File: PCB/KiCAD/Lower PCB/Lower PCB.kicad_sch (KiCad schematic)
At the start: 118 parts, among them IC1 ADG608BRZ, IC2 ADG608BRZ, IC3 ADG608BRZ, J1 Conn_01x04_MountingPin, J2 Conn_01x04_MountingPin, J3 Conn_01x04_MountingPin, J4 Conn_01x02_MountingPin, Q1 SFH320, Q10 SFH320, Q11 SFH320, Q12 SFH320, Q13 SFH320, Q14 SFH320, Q15 SFH320, Q16 SFH320, Q17 SFH320, Q18 SFH320, Q19 SFH320, Q2 SFH320, Q20 SFH320, Q21 SFH320, Q22 SFH320, Q23 SFH320, Q24 SFH320, Q3 SFH320, Q4 SFH320, Q5 SFH320, Q6 SFH320, Q7 SFH320, Q8 SFH320, Q9 SFH320

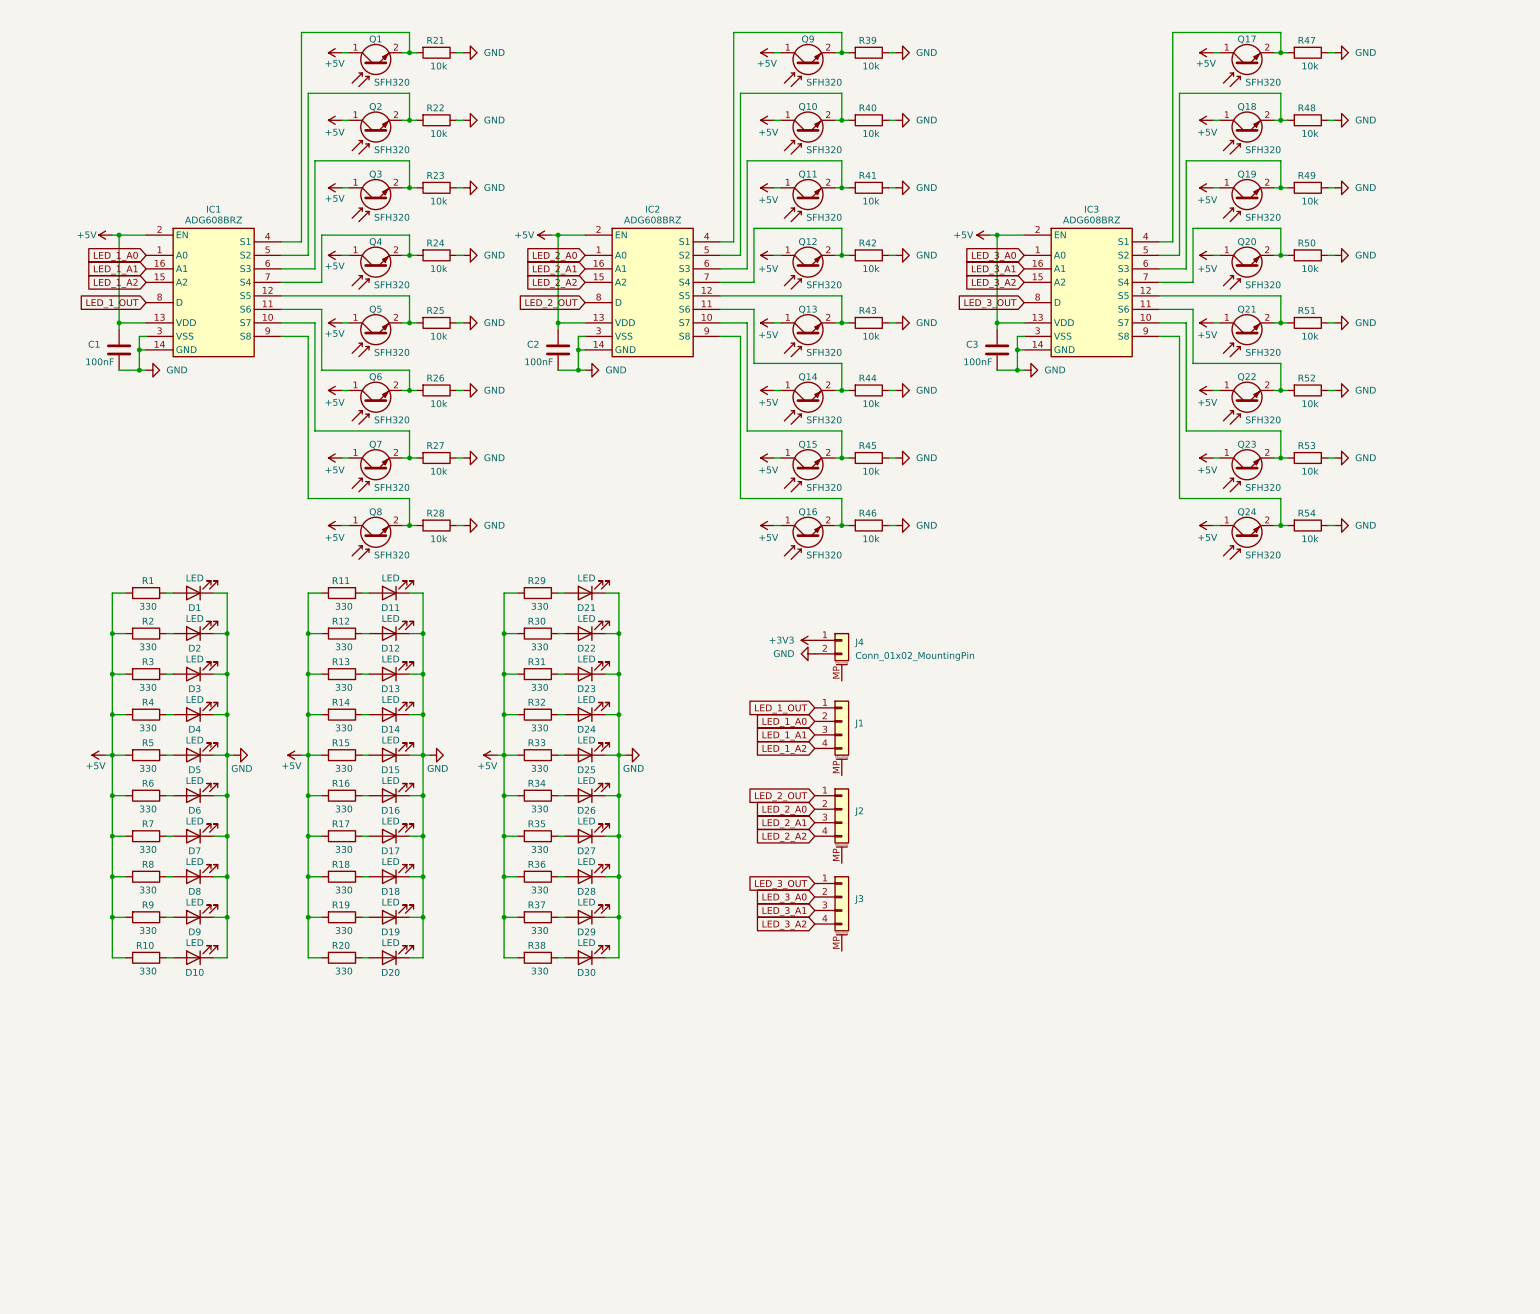
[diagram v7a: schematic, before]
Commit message: More chnages to LED positions and annotations
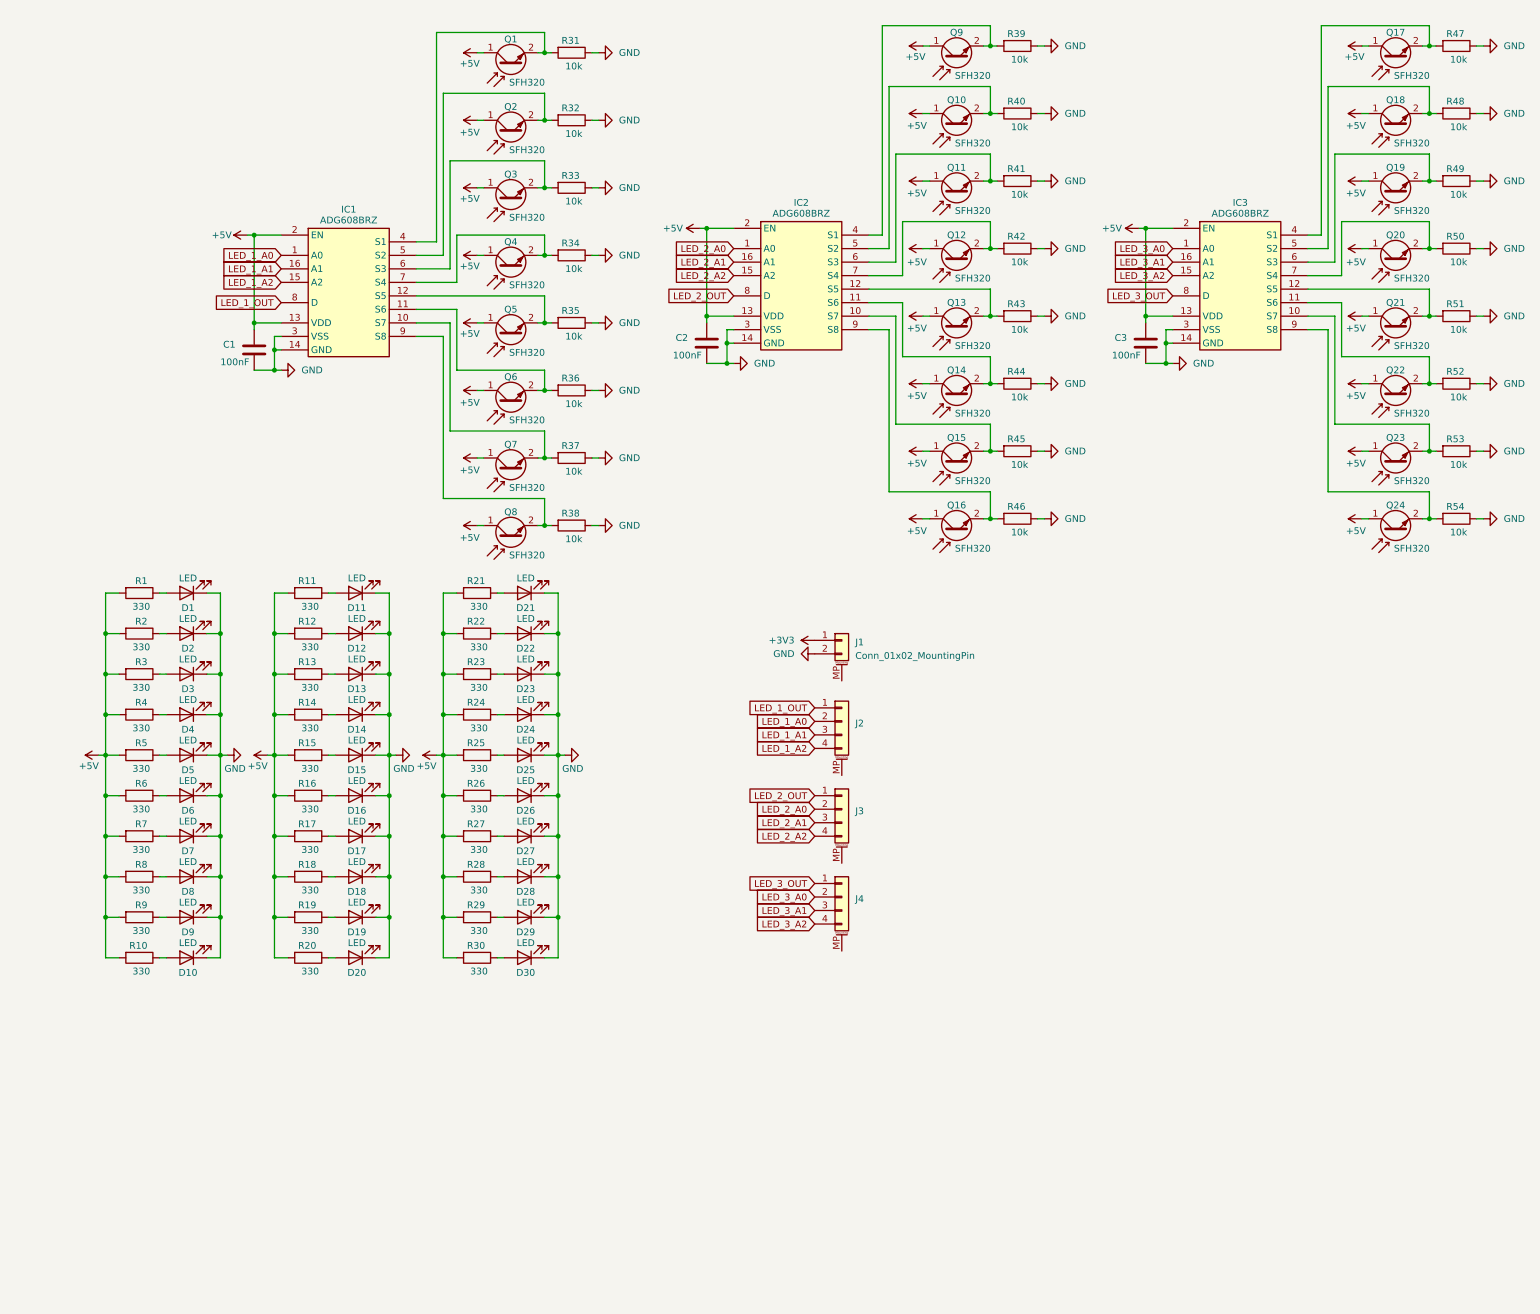
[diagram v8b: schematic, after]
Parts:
- renumbered J4 to J1, J1 to J2, J2 to J3, J3 to J4, R29 to R21, R30 to R22, R31 to R23, R32 to R24, R33 to R25, R34 to R26, R35 to R27, R36 to R28, R37 to R29, R38 to R30, R21 to R31, R22 to R32, R23 to R33, R24 to R34, R25 to R35, R26 to R36, R27 to R37, R28 to R38
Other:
- moved on the sheet: C1, C2, C3, D1, D10, D11, D12, D13, D14, D15, D16, D17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
